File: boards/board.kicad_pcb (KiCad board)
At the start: 2 copper layers, 118 x 70 mm, 61 parts, among them J1 Conn_01x02, J2 Conn_01x02, J3 Conn_01x03, J4 Conn_01x06, J5 Conn_01x05, J6 Conn_01x02, J7 Conn_02x03_Odd_Even, J8 Conn_02x05_Odd_Even, Q1 2N2907, Q2 2n2222, Q3 IRF4905, Q4 2N7000, SW1 Switch, U1 ESP32-WROOM-32U, U2 LM393, U3 LM7805_TO220, U4 LM1117DT-ADJ, U5 LM1117DT-ADJ

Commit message: update PCB and create gerber
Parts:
- C11, C7, C8: footprint Capacitor_THT:CP_Radial_Tantal_D5.5mm_P2.50mm -> easyeda2kicad:CAP-TH_BD5.0-P2.00-D0.8-FD
- C12: footprint Capacitor_THT:CP_Radial_D5.0mm_P2.50mm -> easyeda2kicad:CAP-TH_BD5.0-P2.00-D0.8-FD
- C3: footprint Capacitor_THT:CP_Radial_Tantal_D6.0mm_P2.50mm -> easyeda2kicad:CAP-TH_BD4.0-P1.50-D0.8-FD
- D3: footprint Diode_THT:D_DO-41_SOD81_P10.16mm_Horizontal -> easyeda2kicad:DO-41_BD2.4-L4.7-P8.70-D0.9-RD
- Q1: footprint Package_TO_SOT_THT:TO-92_Inline -> easyeda2kicad:TO-92-3_L4.8-W3.7-P2.54-R
- QRcode git: value LOGO -> LOGO3
- R1, R11, R12, R2, R3, R4, R5, R6, R7, R8: footprint Resistor_THT:R_Axial_DIN0207_L6.3mm_D2.5mm_P7.62mm_Horizontal -> easyeda2kicad:RES-TH_BD2.3-L6.5-P10.50-D0.5
- R10: footprint Resistor_THT:R_Axial_DIN0207_L6.3mm_D2.5mm_P7.62mm_Horizontal -> easyeda2kicad:RES-TH_BD4.5-L11.0-P15.00-D0.7
- R9: value 50k -> 51k; footprint Resistor_THT:R_Axial_DIN0207_L6.3mm_D2.5mm_P7.62mm_Horizontal -> easyeda2kicad:RES-TH_BD2.3-L6.5-P10.50-D0.5
- U1: value ESP32-WROOM-32U -> ESP32-WROOM-32D; footprint RF_Module:ESP32-WROOM-32 -> RF_Module:ESP32-WROOM-32D
- moved R12 37.0 mm to (117.8, 100.5), turned to 90 degrees
- moved C8 34.1 mm to (149.9, 115.6), turned to 0 degrees
- moved U5 31.8 mm to (154.3, 121.0), turned to 180 degrees
- moved TP4 29.2 mm to (160.0, 129.5)
- moved C6 28.8 mm to (102.3, 104.3), turned to 0 degrees
- moved J8 26.1 mm to (134.5, 118.1)
- moved R11 24.0 mm to (122.2, 100.5), turned to -90 degrees
- moved RV3 23.6 mm to (149.2, 130.2), turned to 90 degrees
- moved TP6 22.5 mm to (181.0, 109.8)
- moved R1 21.7 mm to (194.9, 98.4), turned to 90 degrees
- moved J5 21.6 mm to (165.1, 129.5)
- moved C10 21.4 mm to (131.4, 88.4), turned to 90 degrees
- moved TP7 21.3 mm to (181.0, 101.6)
- moved U2 21.1 mm to (198.1, 93.3), turned to 0 degrees
- moved C7 20.5 mm to (156.2, 115.6), turned to 0 degrees
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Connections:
- J8 pad 1: +3V3 -> +5V
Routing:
- net +3V3: track 230.0 -> 180.5 mm, vias 2 -> 1
- net GND: track 480.3 -> 438.3 mm, vias 0 -> 5
- net /V_bat: track 29.8 -> 61.0 mm, vias 1 -> 0
- net +5V: track 206.7 -> 178.0 mm, vias 2 -> 1
- net VSS: track 105.3 -> 78.7 mm, vias 1 -> 0
- net Net-(U2A--): track 29.6 -> 54.6 mm
- net /TDO: track 17.7 -> 41.2 mm, vias 1 -> 0
- net /EN: track 48.0 -> 70.6 mm
- net /DT: track 45.5 -> 28.7 mm
- net /CLK: track 43.5 -> 27.0 mm
- net /TCK: track 17.1 -> 32.9 mm, vias 1 -> 0
- net Net-(D3-A): track 80.2 -> 64.8 mm
- net VDC: track 32.6 -> 47.9 mm, vias 1 -> 0
- net /SCL: track 105.9 -> 91.6 mm
- net /SW: track 48.4 -> 34.9 mm
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- added copper zone on B.Cu, net GND
- added copper zone on F.Cu, net GND
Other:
- board text added: "V_{ss}"
- board text removed: "V_{SS}"

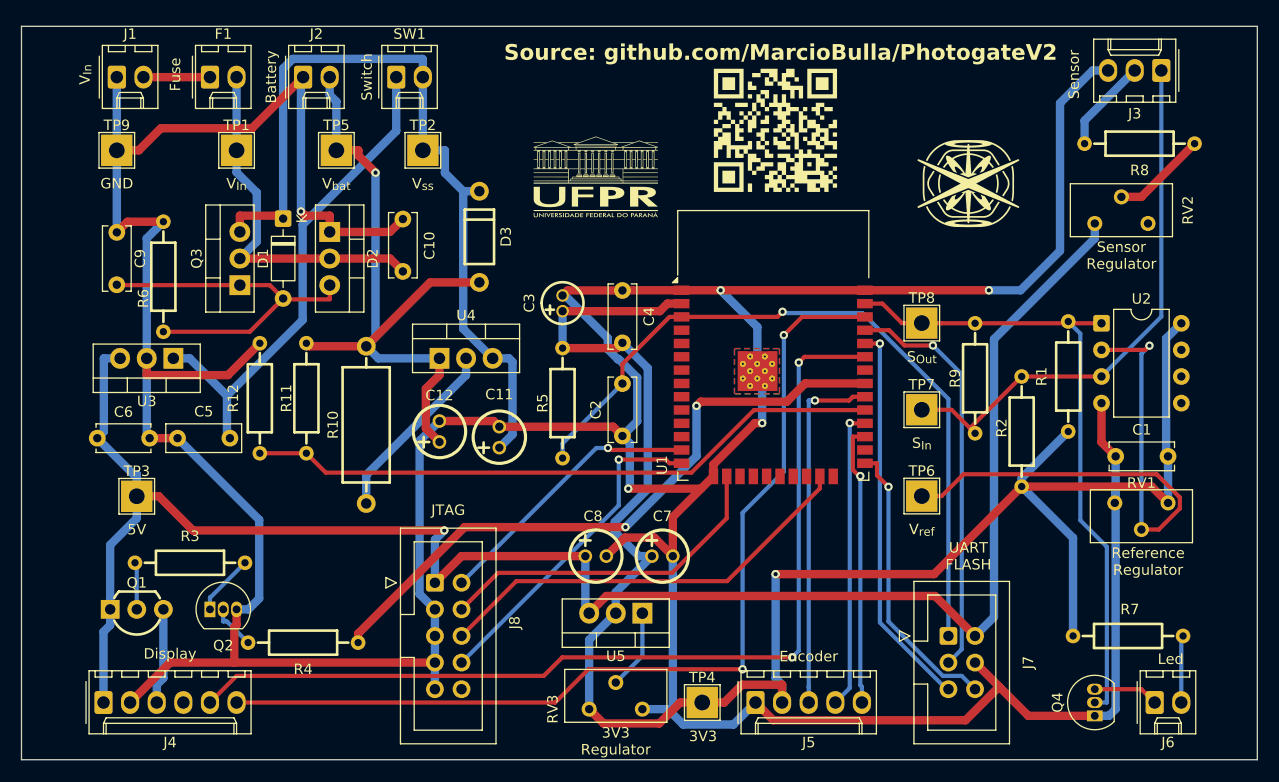
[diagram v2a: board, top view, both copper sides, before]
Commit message: Fiz positon components, add Fabiano seal
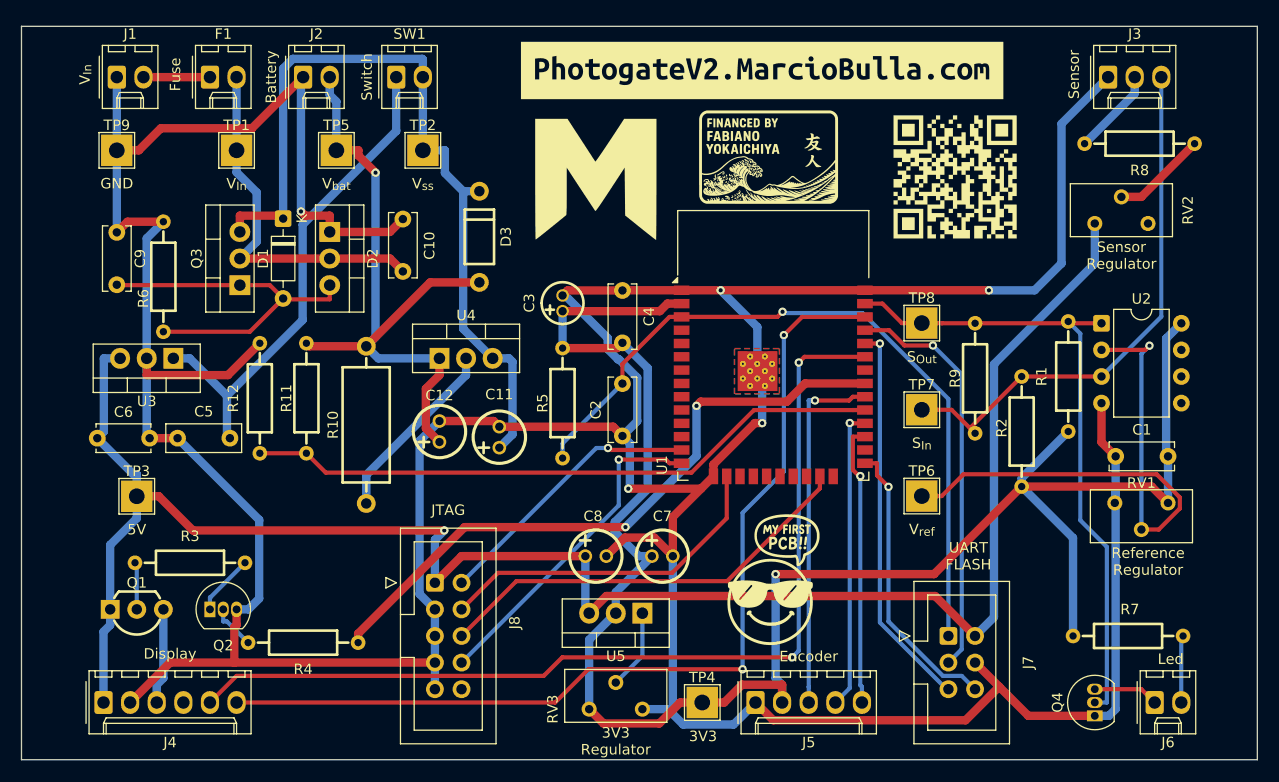
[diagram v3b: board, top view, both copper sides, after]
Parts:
- removed logo1: UFPR, LOGO
- removed logo2: Lorxi, LOGO
- added G*** (x2): LOGO, LOGO, F.Cu at (149.9, 79.4)
- added G***: LOGO, LOGO, F.Cu at (184.2, 79.4)
- added G***: LOGO, LOGO, F.Cu at (166.6, 118.4)
- added G***: LOGO, LOGO, F.Cu at (166.4, 77.5)
- added kibuzzard-689E6D12: G***, kibuzzard-689E6D12, F.Cu at (165.7, 69.2)
- added kibuzzard-689E6DF9: G***, kibuzzard-689E6DF9, F.Cu at (165.7, 69.2)
- moved J3 5.12 mm to (198.8, 69.8), turned to 0 degrees
- moved QRcode git 4.49 mm to (166.4, 79.4)
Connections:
- J3 pad 1: /PH_K -> GND
- J3 pad 3: GND -> /PH_K
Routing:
- net GND: track 438.3 -> 437.6 mm
- net Net-(J3-Pin_2): track 8.97 -> 8.33 mm
- net /PH_K: track 52.2 -> 51.6 mm
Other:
- board text removed: "Source: github.com/MarcioBulla/PhotogateV2"

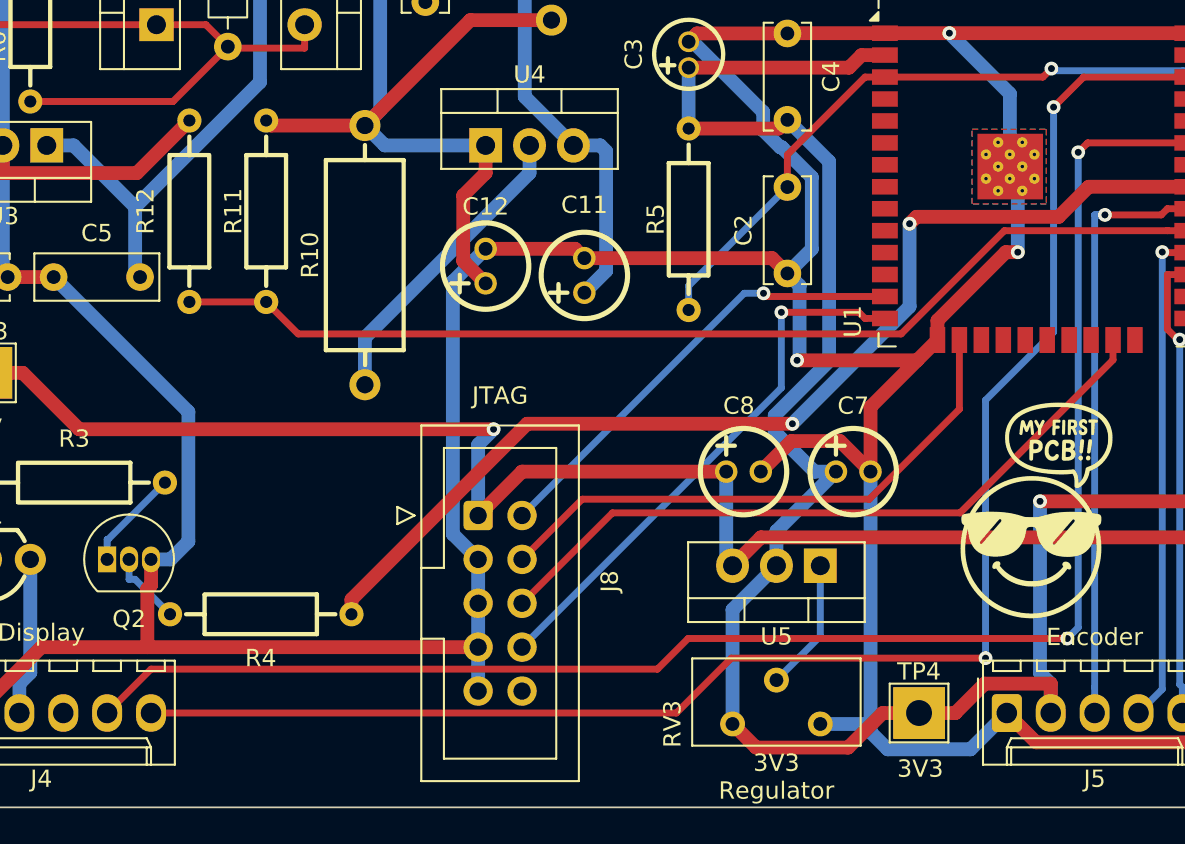
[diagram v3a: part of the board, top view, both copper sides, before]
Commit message: add B.Silkscreen to conn pins
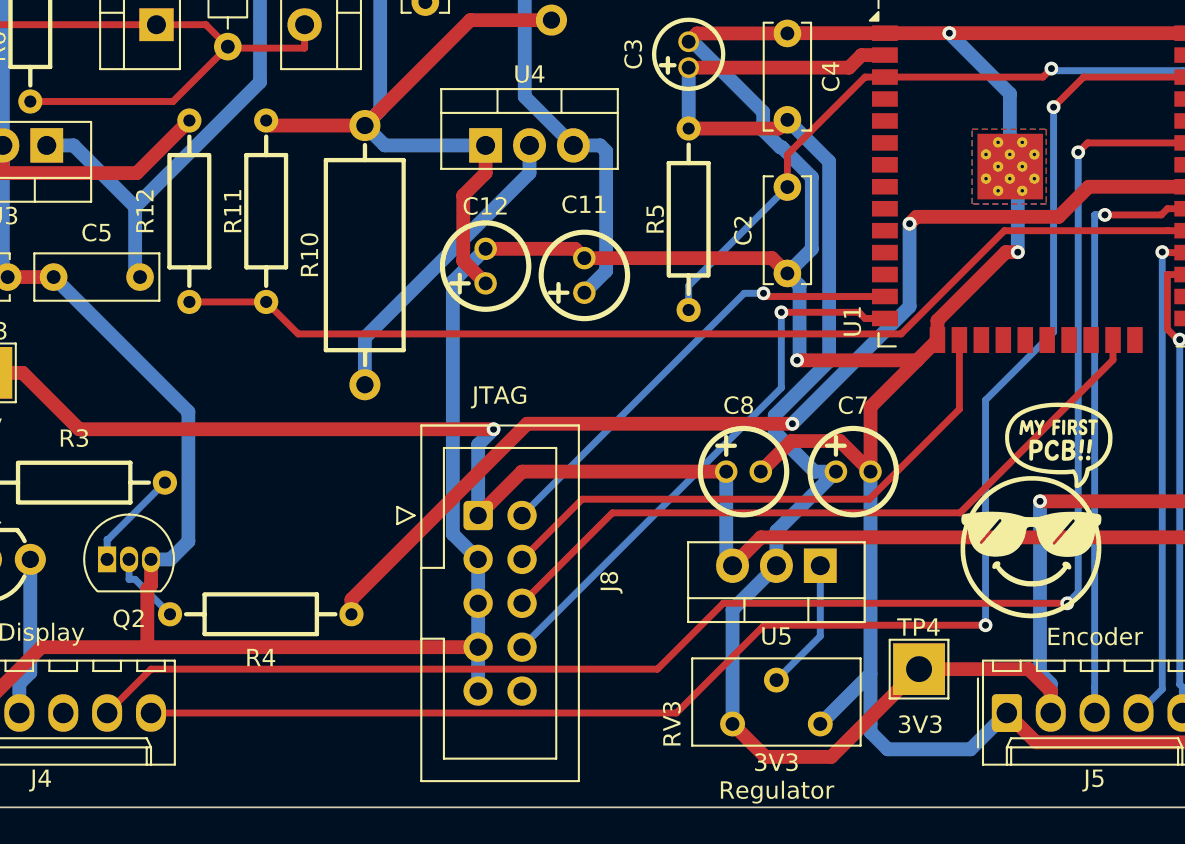
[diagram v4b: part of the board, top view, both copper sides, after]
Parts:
- moved TP4 2.54 mm to (160.0, 127.0)
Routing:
- net GND: track 437.6 -> 438.8 mm
- net /SDA: track 92.3 -> 91.1 mm
- net /SCL: track 91.6 -> 90.5 mm
- net +3V3: track 180.5 -> 181.4 mm
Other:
- board text added: "+"
- board text added: "-"
- board text added: "CLK"
- board text added: "DT"
- board text added: "K"
- board text added: "PWM"
- board text added: "SCL"
- board text added: "SDA"
- board text added: "SW"
